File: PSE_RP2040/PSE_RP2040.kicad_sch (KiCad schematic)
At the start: 68 parts, among them IC2 SAM-M8Q-0, J1 USB_B, J2 USB_B_Micro, J3 8P8C_LED, J4 Conn_01x03, Q1 DTC114Y, Q2 Q_PMOS_GSD, SW1 SW_Push, U1 RP2040, U2 PCF8563T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

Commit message: assegnamento footprint PAM7Q
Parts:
- C1, C4: footprint (none) -> Capacitor_SMD:C_0805_2012Metric
- C10, C11, C13, C15, C3, C36, C6, C7, C8, C9: footprint (none) -> Capacitor_SMD:C_0603_1608Metric
- J1: footprint (none) -> Connector_USB:USB_B_OST_USB-B1HSxx_Horizontal
- L1: footprint (none) -> Inductor_SMD:L_0603_1608Metric
- R1, R11, R12, R13, R2, R27, R28, R3, R36, R4, R5, R6, R7: footprint (none) -> Resistor_SMD:R_0603_1608Metric
- SW1: footprint (none) -> Button_Switch_SMD:SW_SPST_EVQP0
- TP1: value (none) -> 3V3; footprint (none) -> TestPoint:TestPoint_Keystone_5005-5009_Compact
- TP10: value (none) -> UART_RX-GPS_TX
- TP11: value (none) -> VCC
- TP12: value (none) -> I2C_SCL_RTC
- TP13: value (none) -> I2C_SDA_RTC
- TP2: value (none) -> GND; footprint (none) -> TestPoint:TestPoint_Keystone_5005-5009_Compact
- TP3: value (none) -> 5V; footprint (none) -> TestPoint:TestPoint_Keystone_5005-5009_Compact
- TP4: value (none) -> 1V1
- TP5: value (none) -> POE+; footprint (none) -> TestPoint:TestPoint_Keystone_5005-5009_Compact
- TP6: value (none) -> POE-; footprint (none) -> TestPoint:TestPoint_Keystone_5005-5009_Compact
- TP7: value (none) -> USB_DP
- TP8: value (none) -> USB_DN
- TP9: value (none) -> UART_TX-GPS_RX

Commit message: footprint flash
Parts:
- removed U3: W25Q32JVSS, Package_SO:SOIC-8_5.23x5.23mm_P1.27mm, symbol Memory_Flash:W25Q32JVSS
- U6: footprint (none) -> PSE2021:PAM-7Q
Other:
- moved on the sheet: C15, C18, R11, R28, SW1, U5

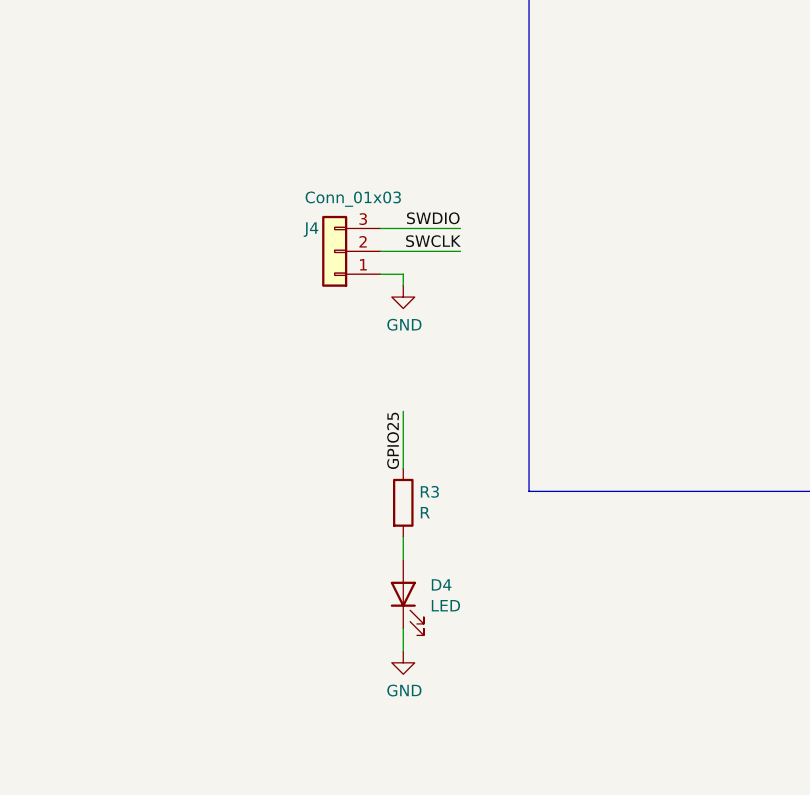
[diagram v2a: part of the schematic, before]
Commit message: footprint usb micro e crystal
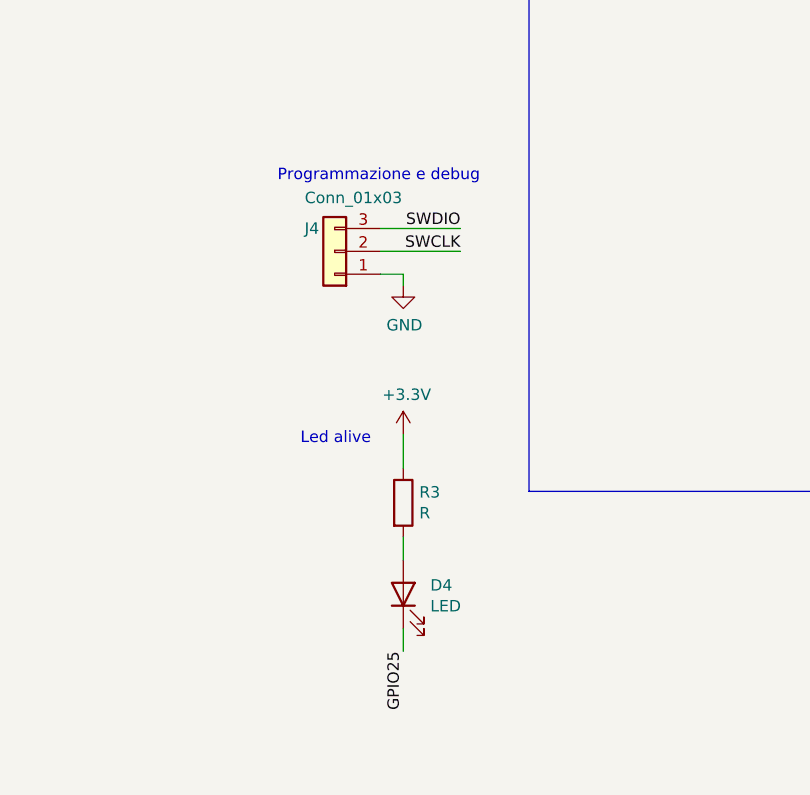
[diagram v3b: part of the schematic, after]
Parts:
- U5: footprint (none) -> Package_SO:SOIC-8_5.23x5.23mm_P1.27mm
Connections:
- net +3V3: now also R3.1
- net GND: no longer D4.1 (K)
- net GPIO25: now also D4.1 (K); no longer R3.1
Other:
- note added: "Led alive"
- note added: "Programmazione e debug"
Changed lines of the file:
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@@
     (stroke (width 0) (type default) (color 0 0 0 0))
   )
-  (wire (pts (xy 285.75 250.19) (xy 285.75 243.84))
+  (wire (pts (xy 285.75 250.19) (xy 285.75 246.38))
     (stroke (width 0) (type default) (color 0 0 0 0))
   )
@@
     (effects (font (size 1.27 1.27)) (justify left bottom))
   )
+  (text "Led alive" (at 274.32 247.65 0)
+    (effects (font (size 1.27 1.27)) (justify left bottom))
+  )
+  (text "Programmazione e debug" (at 271.78 218.44 0)
+    (effects (font (size 1.27 1.27)) (justify left bottom))
+  )
   (text "Testpoint" (at 13.97 179.07 0)
     (effects (font (size 1.27 1.27)) (justify left bottom))
@@
     (effects (font (size 1.27 1.27)) (justify right bottom))
   )
-  (label "GPIO25" (at 285.75 243.84 270)
-    (effects (font (size 1.27 1.27)) (justify right bottom))
-  )
   (label "GPIO9" (at 162.56 53.34 180)
     (effects (font (size 1.27 1.27)) (justify right bottom))
@@
     (effects (font (size 1.27 1.27)) (justify left bottom))
   )
+  (label "GPIO25" (at 285.75 270.51 270)
+    (effects (font (size 1.27 1.27)) (justify right bottom))
+  )
   (label "GPIO25" (at 223.52 76.2 0)
     (effects (font (size 1.27 1.27)) (justify left bottom))
@@
     (property "Reference" "U5" (id 0) (at 345.44 50.419 0))
     (property "Value" "W25Q16JVUXIQ" (id 1) (at 345.44 52.7304 0))
-    (property "Footprint" "" (id 2) (at 341.63 63.5 0)
+    (property "Footprint" "Package_SO:SOIC-8_5.23x5.23mm_P1.27mm" (id 2) (at 341.63 63.5 0)
       (effects (font (size 1.27 1.27)) hide)
     )
@@
     (pin "2")
   )
-  (symbol (lib_id "power:GND") (at 285.75 270.51 0) (unit 1)
-    (in_bom yes) (on_board yes)
-    (property "Reference" "#PWR0118" (id 0) (at 285.75 276.86 0)
-      (effects (font (size 1.27 1.27)) hide)
-    )
-    (property "Value" "GND" (id 1) (at 285.877 274.9042 0))
-    (property "Footprint" "" (id 2) (at 285.75 270.51 0)
-      (effects (font (size 1.27 1.27)) hide)
-    )
-    (property "Datasheet" "" (id 3) (at 285.75 270.51 0)
-      (effects (font (size 1.27 1.27)) hide)
-    )
-    (pin "1")
-  )
   (symbol (lib_id "Device:LED") (at 285.75 264.16 90) (unit 1)
     (in_bom yes) (on_board yes)
@@
     (pin "3")
   )
+  (symbol (lib_id "power:+3.3V") (at 285.75 246.38 0) (unit 1)
+    (in_bom yes) (on_board yes)
+    (property "Reference" "#PWR0118" (id 0) (at 285.75 250.19 0)
+      (effects (font (size 1.27 1.27)) hide)
+    )
+    (property "Value" "+3.3V" (id 1) (at 286.131 241.9858 0))
+    (property "Footprint" "" (id 2) (at 285.75 246.38 0)
+      (effects (font (size 1.27 1.27)) hide)
+    )
+    (property "Datasheet" "" (id 3) (at 285.75 246.38 0)
+      (effects (font (size 1.27 1.27)) hide)
+    )
+    (pin "1")
+  )
   (symbol (lib_id "power:PWR_FLAG") (at 59.69 31.75 0) (unit 1)
     (in_bom yes) (on_board yes) (fields_autoplaced)
@@
       (reference "#PWR0117") (unit 1) (value "+3.3V") (footprint "")
     )
-    (path "/00000000-0000-0000-0000-000062815729"
-      (reference "#PWR0118") (unit 1) (value "GND") (footprint "")
+    (path "/89540d80-e45e-4a11-a899-5fb580f15d37"
+      (reference "#PWR0118") (unit 1) (value "+3.3V") (footprint "")
     )
     (path "/00000000-0000-0000-0000-000062729871"
@@
     )
     (path "/7469ee59-99c2-4fbc-bbf0-68001b2365d4"
-      (reference "J2") (unit 1) (value "USB_B_Micro") (footprint "")
+      (reference "J2") (unit 1) (value "USB_B_Micro") (footprint "Connector_USB:USB_Micro-B_Wuerth_629105150521")
     )
     (path "/bf0d8b7c-a679-427a-a45f-7cba44734d82"
@@
     )
     (path "/fcbec5fb-5634-49d7-ab3e-008c50bb3423/3930f427-f405-499d-a361-a0261363df3a"
-      (reference "T1") (unit 1) (value "749013011") (footprint "")
+      (reference "T1") (unit 1) (value "749013011") (footprint "Transformer_SMD:Transformer_Ethernet_Wuerth_749013011A")
     )
     (path "/0a8ea5bc-4cec-47a7-ad41-220b78ea6d5a"
@@
     )
     (path "/b11e24a5-0ab3-45be-bace-0e8623fdcceb"
-      (reference "Y1") (unit 1) (value "Crystal_GND3") (footprint "")
+      (reference "Y1") (unit 1) (value "Crystal_GND3") (footprint "Crystal:Crystal_AT310_D3.0mm_L10.0mm_Horizontal_1EP_style1")
     )
     (path "/00000000-0000-0000-0000-00006234c592"
-      (reference "Y2") (unit 1) (value "Crystal_GND24") (footprint "")
+      (reference "Y2") (unit 1) (value "Crystal_GND24") (footprint "Crystal:Crystal_SMD_3225-4Pin_3.2x2.5mm")
     )
     (path "/fcbec5fb-5634-49d7-ab3e-008c50bb3423/ed250987-5744-495f-bb1e-2798bdb55393"

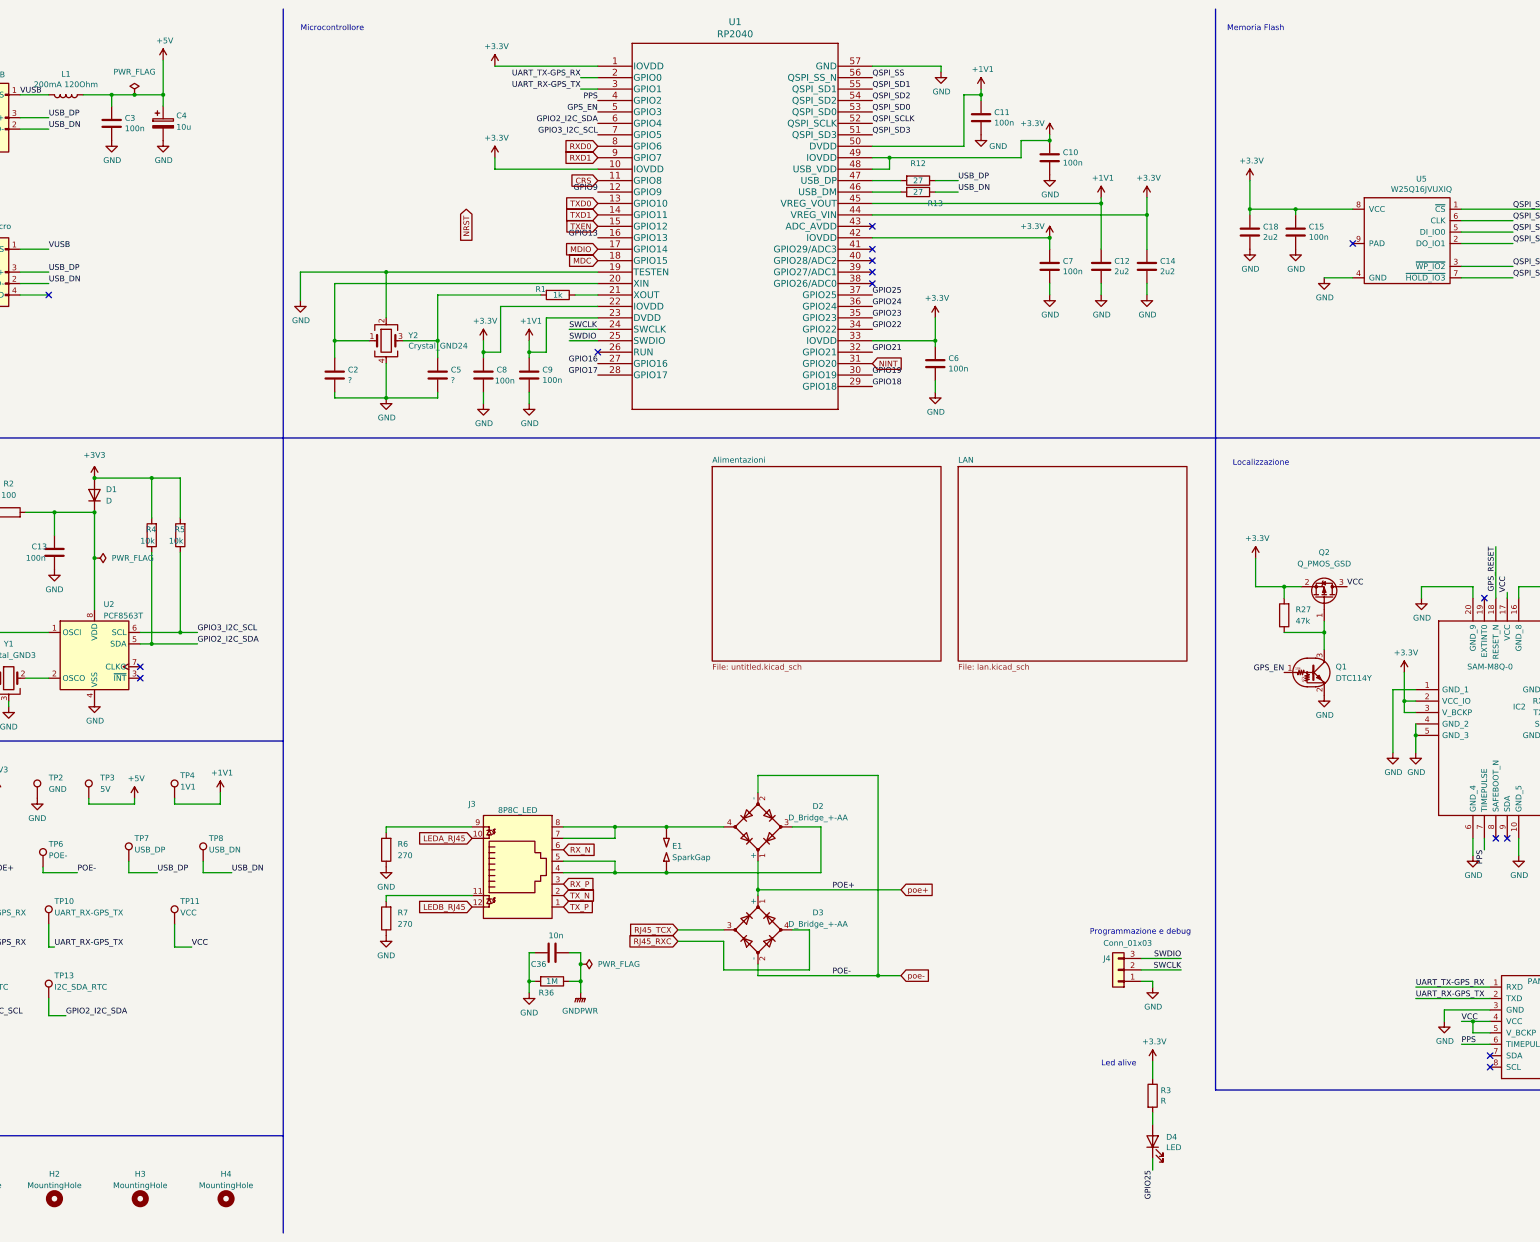
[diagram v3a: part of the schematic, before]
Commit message: footprint, aggiunto bottone rst
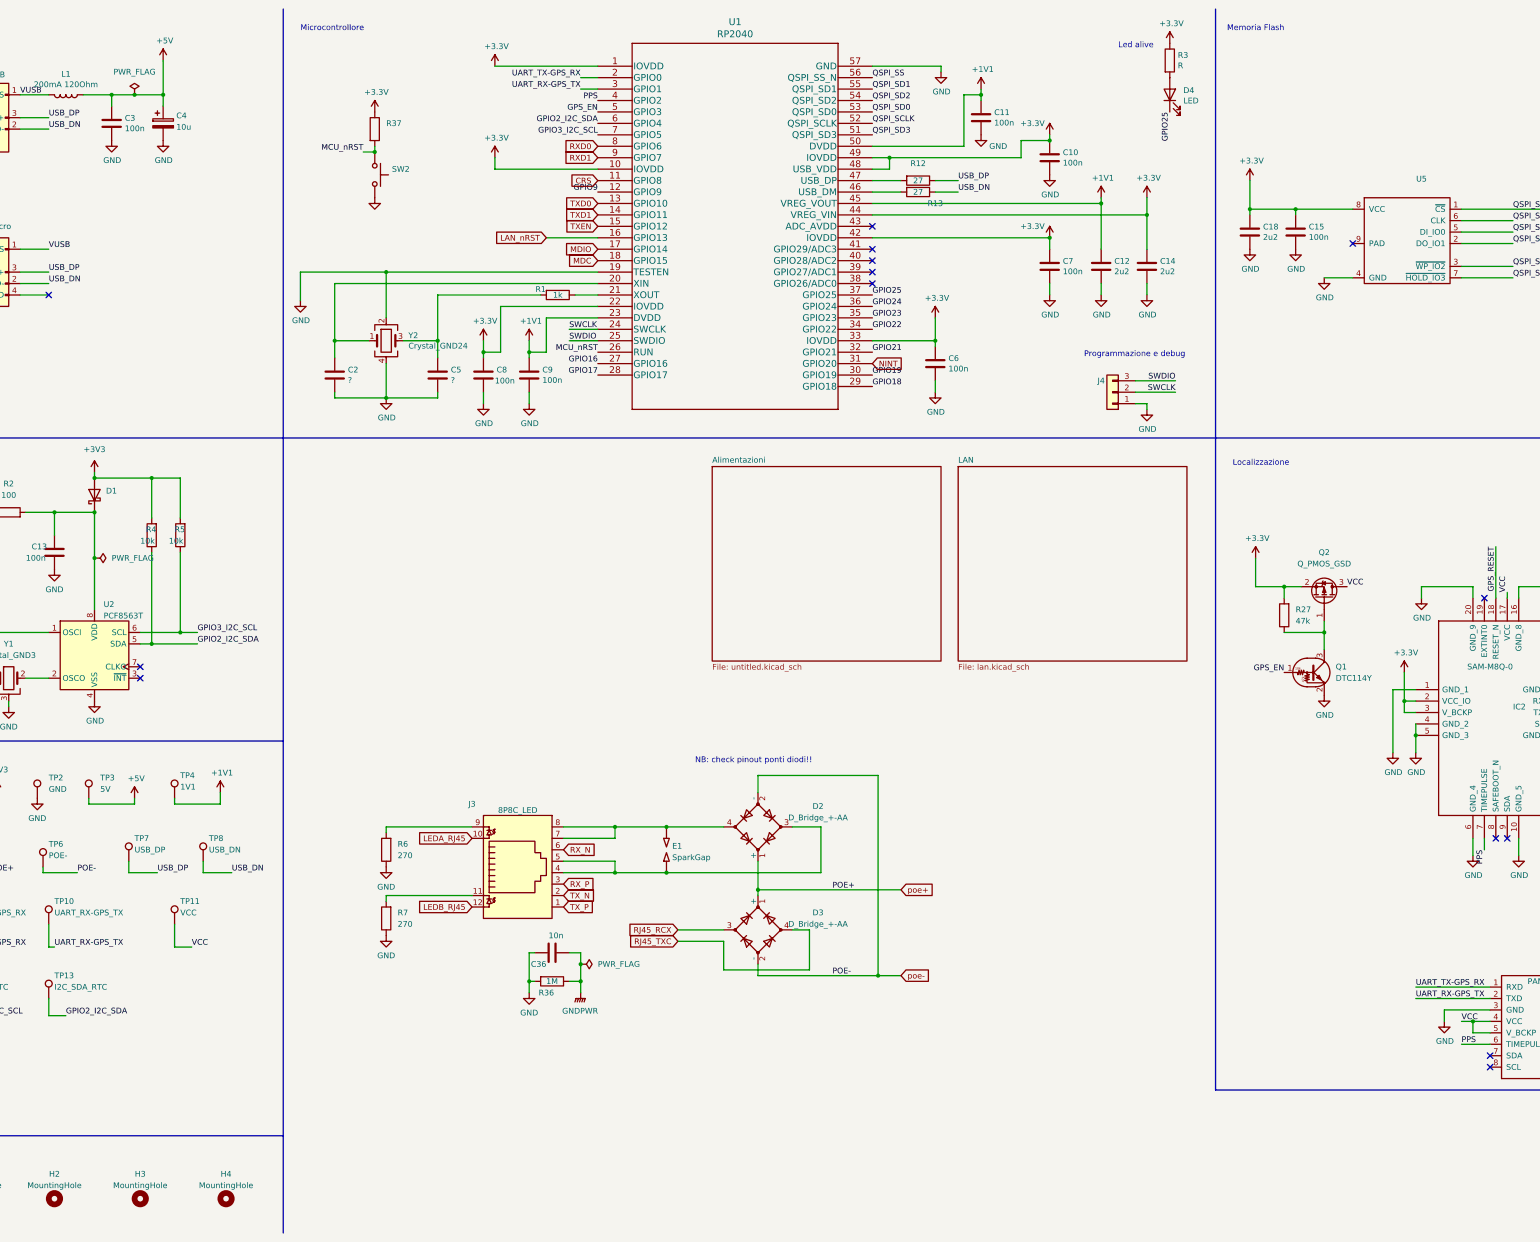
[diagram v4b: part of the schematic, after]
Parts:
- removed D1: D, symbol Device:D
- added D1: (no value), symbol Device:D_Schottky
- added R37: (no value), symbol Device:R
- added SW2: (no value), symbol Switch:SW_Push
- J2: footprint (none) -> Connector_USB:USB_Micro-B_Wuerth_629105150521
- J4: value Conn_01x03 -> (none)
- U5: value W25Q16JVUXIQ -> (none); footprint Package_SO:SOIC-8_5.23x5.23mm_P1.27mm -> (none)
- Y1: footprint (none) -> Crystal:Crystal_AT310_D3.0mm_L10.0mm_Horizontal_1EP_style1
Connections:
- net +3V3: now also D1.2 (A), R37.1
- net GND: now also SW2.2
- net MCU_nRST: now reaches U1.26 (RUN)
- net MCU_nRST: now also R37.2, SW2.1
- net at C13.1, R2.2, U2.8 (VDD): now also D1.1 (K)
- net GPIO13 renamed LAN_nRST
- net RJ45_RXC renamed RJ45_TXC
- net RJ45_TCX renamed RJ45_RCX
- no-connect marks 16 -> 15
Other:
- note added: "NB: check pinout ponti diodi!!"
- moved on the sheet: D4, J4, R3
